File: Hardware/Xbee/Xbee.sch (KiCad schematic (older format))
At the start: 39 parts, among them J1 Alimentación, J2 Raspberry, J3 Pines 1, J4 Pines 2, J5 Programación, J6 Entrada, J7 Salida, J8 Batería, K1 SANYOU_SRD_Form_C, Q1 2N7002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

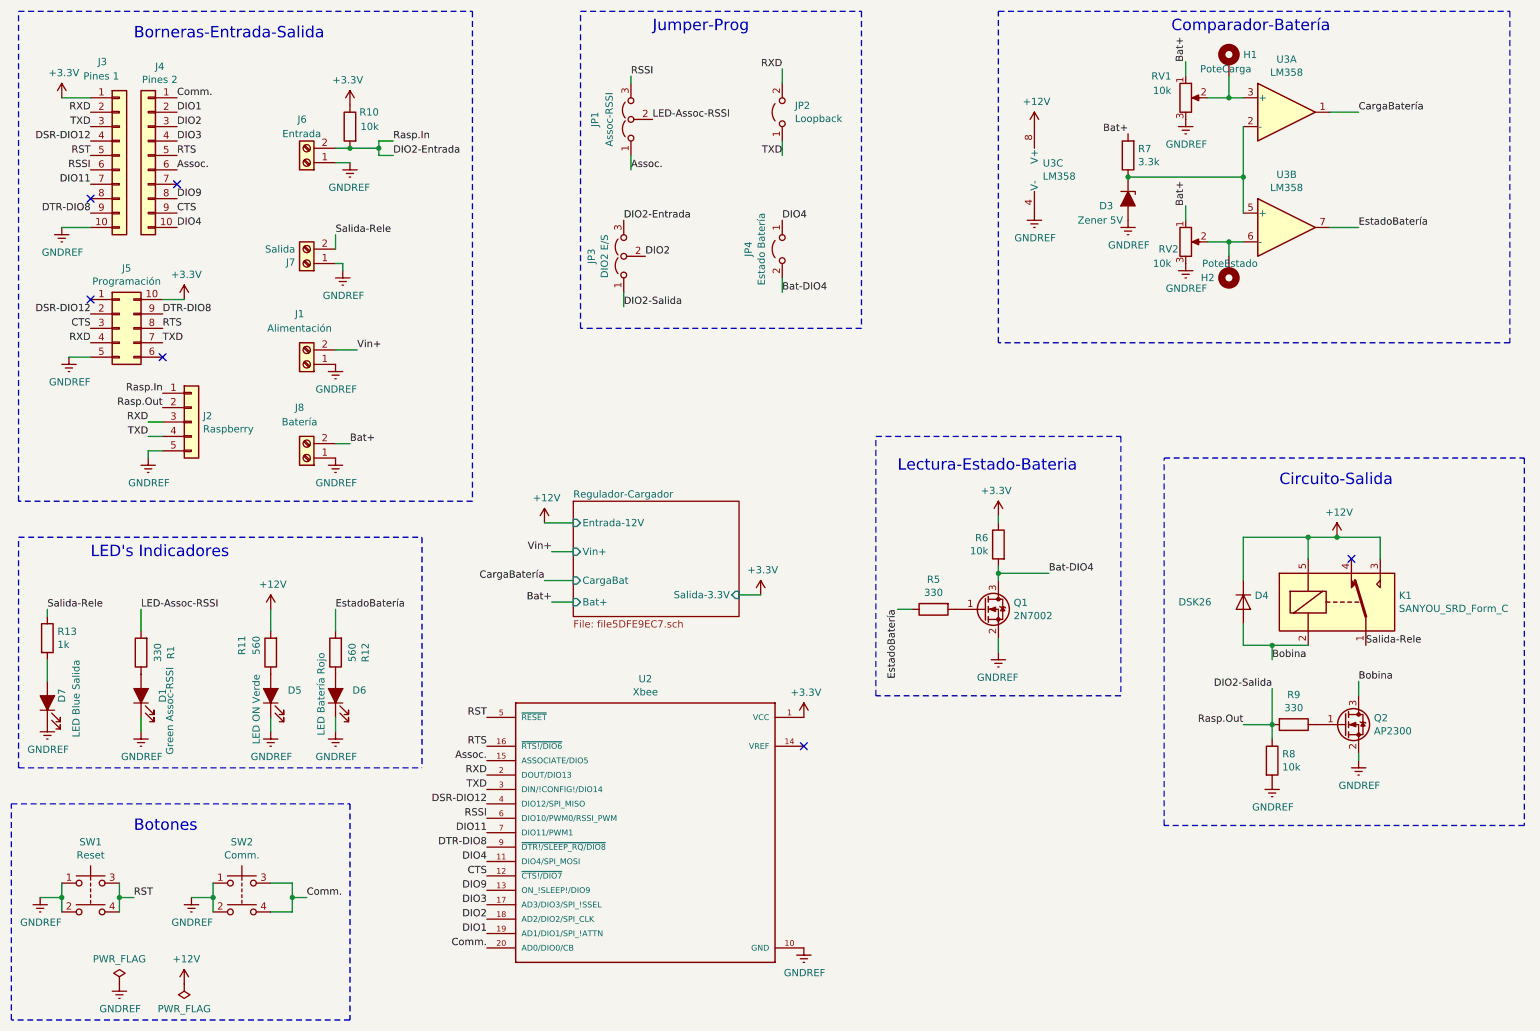
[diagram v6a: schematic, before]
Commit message: Change footprints 2
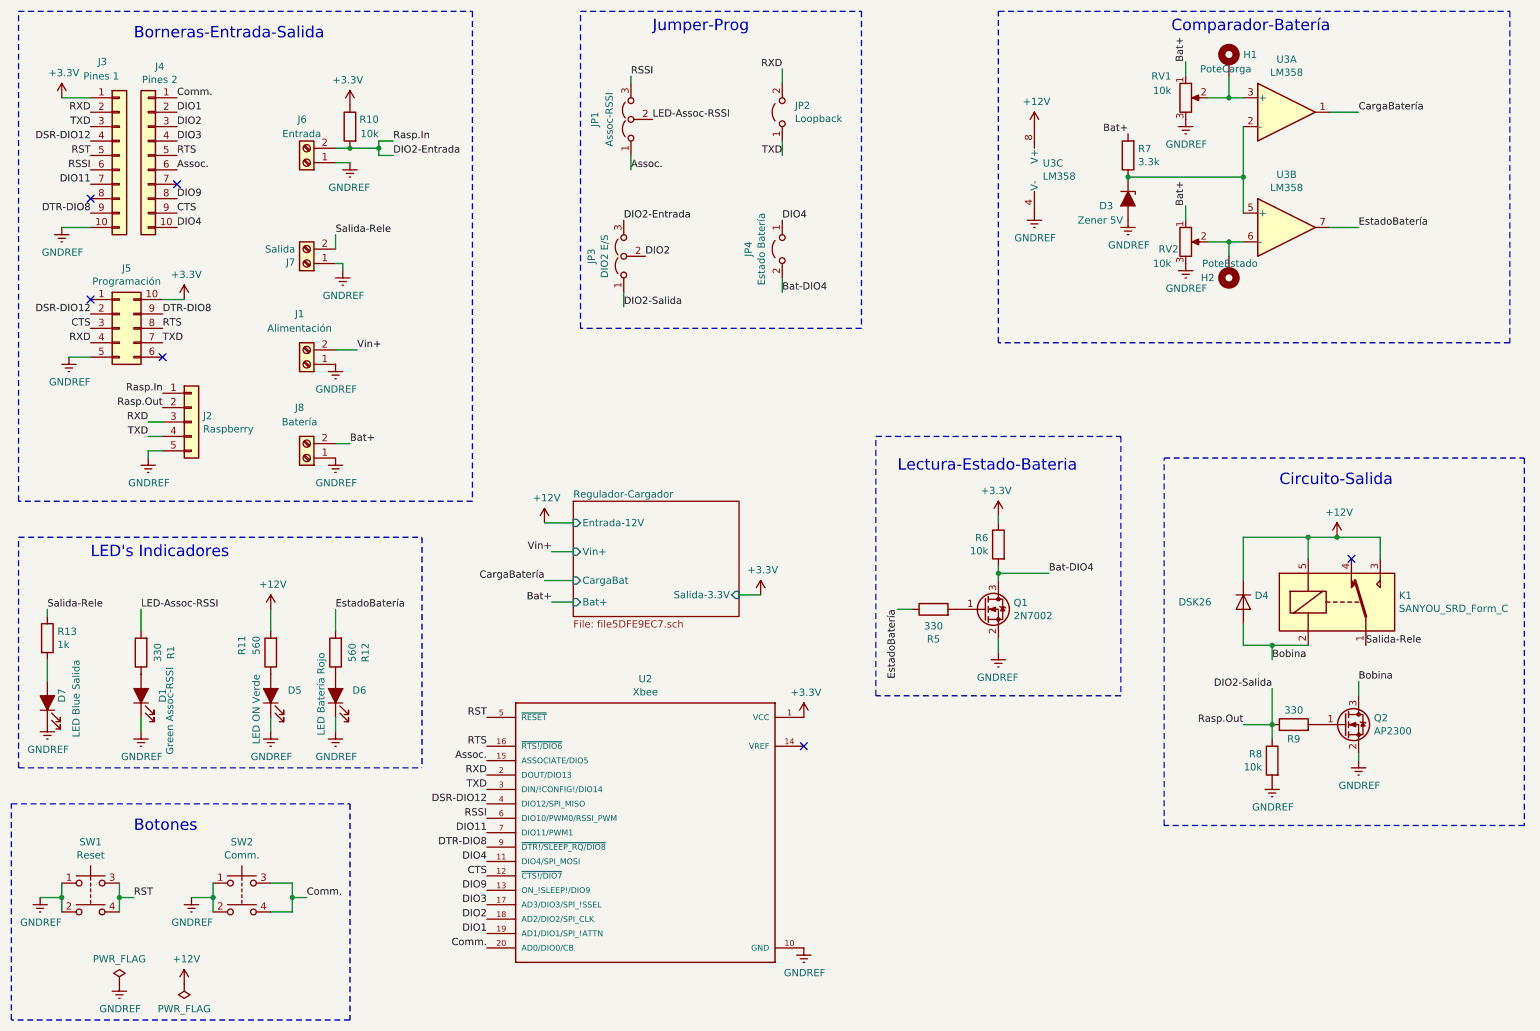
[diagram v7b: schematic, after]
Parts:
- D3: Código Proveedor 1 (none) -> 1727-5167-2-ND; Link Proveedor 1 (none) -> https://www.digikey.com/product-detail/es/nexperia-usa-inc/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; Nombre Fabricante (none) -> PLVA650A,215; Package (none) -> SOT-23
- Q1, Q2: Código Proveedor 1 (none) -> 2N7002NCT-ND; Link Proveedor 1 (none) -> https://www.digikey.com/product-detail/es/on-semiconductor/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; Nombre Fabricante (none) -> 2N7002; Package (none) -> SOT-23
- R10, R8: footprint Resistor_SMD:R_0805_2012Metric_Pad1.15x1.40mm_HandSolder -> Resistor_SMD:R_1206_3216Metric_Pad1.42x1.75mm_HandSolder; Código Proveedor 1 (none) -> 311-10KERCT-ND; Link Proveedor 1 (none) -> https://www.digikey.com/product-detail/en/yageo/RC1206JR-07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; Nombre Fabricante (none) -> RC1206JR-0710KL; Package (none) -> 1206
- R5, R9: footprint Resistor_SMD:R_0805_2012Metric_Pad1.15x1.40mm_HandSolder -> Resistor_SMD:R_1206_3216Metric_Pad1.42x1.75mm_HandSolder; Código Proveedor 1 (none) -> P.33PCT-ND; Link Proveedor 1 (none) -> https://www.digikey.com/product-detail/en/panasonic-electro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; Nombre Fabricante (none) -> ERJ-8RQJR33V; Package (none) -> 1206
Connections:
- net DIO2-Salida: now also R9.1; no longer R9.2
- net at Q2.1 (G): now also R9.2; no longer R9.1
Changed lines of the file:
@@
 EESchema Schematic File Version 4
 LIBS:Xbee-cache
-EELAYER 30 0
+EELAYER 29 0
 EELAYER END
 $Descr A4 11693 8268
@@
 F 2 "Diode_SMD:D_SOT-23_ANK" H 8350 1950 50  0001 C CNN
 F 3 "~" H 8350 1950 50  0001 C CNN
+F 4 "https://www.digikey.com/product-detail/es/nexperia-usa-inc/PLVA650A215/1727-5167-2-ND/1163688" H 8350 1950 50  0001 C CNN "Link Proveedor 1"
+F 5 "SOT-23" H 8350 1950 50  0001 C CNN "Package"
+F 6 "1727-5167-2-ND " H 8350 1950 50  0001 C CNN "Código Proveedor 1"
+F 7 "PLVA650A,215" H 8350 1950 50  0001 C CNN "Nombre Fabricante"
 	1    8350 1950
 	0    1    1    0
@@
 Wire Wire Line
 	7450 5100 7450 5000
-$Comp
-L Xbee-rescue:R-Device R5
-U 1 1 5C1B535E
-P 7000 4800
-F 0 "R5" V 6793 4800 50  0000 C CNN
-F 1 "330" V 6884 4800 50  0000 C CNN
-F 2 "Resistor_SMD:R_0805_2012Metric_Pad1.15x1.40mm_HandSolder" V 6930 4800 50  0001 C CNN
-F 3 "~" H 7000 4800 50  0001 C CNN
-	1    7000 4800
-	0    -1   1    0
-$EndComp
 Text Label 9950 2150 0    50   ~ 0
 EstadoBatería
@@
 Text Label 1750 1250 0    50   ~ 0
 Comm.
-$Comp
-L Xbee-rescue:R-Device R10
-U 1 1 5C1C2E7B
-P 2950 1450
-F 0 "R10" H 2750 1550 50  0000 L CNN
-F 1 "10k" H 2750 1450 50  0000 L CNN
-F 2 "Resistor_SMD:R_0805_2012Metric_Pad1.15x1.40mm_HandSolder" V 2880 1450 50  0001 C CNN
-F 3 "~" H 2950 1450 50  0001 C CNN
-	1    2950 1450
-	-1   0    0    -1
-$EndComp
 $Comp
 L Xbee-rescue:+3.3V-power #PWR032
@@
 	1    4850 2350
 	0    -1   -1   0
-$EndComp
-$Comp
-L Xbee-rescue:R-Device R9
-U 1 1 5C1D0264
-P 9500 5600
-F 0 "R9" V 9293 5600 50  0000 C CNN
-F 1 "330" V 9384 5600 50  0000 C CNN
-F 2 "Resistor_SMD:R_0805_2012Metric_Pad1.15x1.40mm_HandSolder" V 9430 5600 50  0001 C CNN
-F 3 "~" H 9500 5600 50  0001 C CNN
-	1    9500 5600
-	0    1    1    0
 $EndComp
 Wire Wire Line
@@
 	9150 5050 9350 5050
 $Comp
-L Xbee-rescue:R-Device R8
-U 1 1 5C89E422
-P 9350 5850
-F 0 "R8" H 9420 5896 50  0000 L CNN
-F 1 "10k" H 9420 5805 50  0000 L CNN
-F 2 "Resistor_SMD:R_0805_2012Metric_Pad1.15x1.40mm_HandSolder" V 9280 5850 50  0001 C CNN
-F 3 "~" H 9350 5850 50  0001 C CNN
-	1    9350 5850
-	1    0    0    -1
-$EndComp
-$Comp
 L Xbee-rescue:GNDREF-power #PWR027
 U 1 1 5C89E4B4
@@
 F 2 "Package_TO_SOT_SMD:SOT-23" H 7550 4725 50  0001 L CIN
 F 3 "https://www.fairchildsemi.com/datasheets/2N/2N7002.pdf" H 7350 4800 50  0001 L CNN
+F 4 "2N7002" H 7350 4800 50  0001 C CNN "Nombre Fabricante"
+F 5 "2N7002NCT-ND" H 7350 4800 50  0001 C CNN "Código Proveedor 1"
+F 6 "SOT-23" H 7350 4800 50  0001 C CNN "Package"
+F 7 "https://www.digikey.com/product-detail/es/on-semiconductor/2N7002/2N7002NCT-ND/244664" H 7350 4800 50  0001 C CNN "Link Proveedor 1"
 	1    7350 4800
 	1    0    0    -1
@@
 F 2 "Package_TO_SOT_SMD:SOT-23" H 10050 5525 50  0001 L CIN
 F 3 "https://www.fairchildsemi.com/datasheets/2N/2N7002.pdf" H 9850 5600 50  0001 L CNN
+F 4 "https://www.digikey.com/product-detail/es/on-semiconductor/2N7002/2N7002NCT-ND/244664" H 9850 5600 50  0001 C CNN "Link Proveedor 1"
+F 5 "SOT-23" H 9850 5600 50  0001 C CNN "Package"
+F 6 "2N7002" H 9850 5600 50  0001 C CNN "Nombre Fabricante"
+F 7 "2N7002NCT-ND" H 9850 5600 50  0001 C CNN "Código Proveedor 1"
 	1    9850 5600
 	1    0    0    -1
@@
 Wire Wire Line
 	3150 1650 3150 1600
-Connection ~ 2950 1600
-Wire Wire Line
-	2950 1600 2850 1600
-Wire Wire Line
-	3150 1600 2950 1600
 Connection ~ 3150 1600
 Wire Wire Line
@@
 Wire Wire Line
 	2850 4800 2850 4950
+$Comp
+L Xbee-rescue:R-Device R5
+U 1 1 5DB489D4
+P 7000 4800
+F 0 "R5" V 6793 4800 50  0000 C CNN
+F 1 "330" V 6884 4800 50  0000 C CNN
+F 2 "Resistor_SMD:R_1206_3216Metric_Pad1.42x1.75mm_HandSolder" V 6930 4800 50  0001 C CNN
+F 3 "~" H 7000 4800 50  0001 C CNN
+F 4 "ERJ-8RQJR33V" H 7000 4800 50  0001 C CNN "Nombre Fabricante"
+F 5 "P.33PCT-ND" H 7000 4800 50  0001 C CNN "Código Proveedor 1"
+F 6 "https://www.digikey.com/product-detail/en/panasonic-electronic-components/ERJ-8RQJR33V/P.33PCT-ND/250371" H 7000 4800 50  0001 C CNN "Link Proveedor 1"
+F 7 "1206" H 7000 4800 50  0001 C CNN "Package"
+	1    7000 4800
+	0    -1   -1   0
+$EndComp
+$Comp
+L Xbee-rescue:R-Device R9
+U 1 1 5DB4C324
+P 9500 5600
+F 0 "R9" V 9400 5600 50  0000 C CNN
+F 1 "330" V 9600 5600 50  0000 C CNN
+F 2 "Resistor_SMD:R_1206_3216Metric_Pad1.42x1.75mm_HandSolder" V 9430 5600 50  0001 C CNN
+F 3 "~" H 9500 5600 50  0001 C CNN
+F 4 "ERJ-8RQJR33V" H 9500 5600 50  0001 C CNN "Nombre Fabricante"
+F 5 "P.33PCT-ND" H 9500 5600 50  0001 C CNN "Código Proveedor 1"
+F 6 "https://www.digikey.com/product-detail/en/panasonic-electronic-components/ERJ-8RQJR33V/P.33PCT-ND/250371" H 9500 5600 50  0001 C CNN "Link Proveedor 1"
+F 7 "1206" H 9500 5600 50  0001 C CNN "Package"
+	1    9500 5600
+	0    -1   -1   0
+$EndComp
+$Comp
+L Xbee-rescue:R-Device R8
+U 1 1 5DB4D079
+P 9350 5850
+F 0 "R8" H 9420 5896 50  0000 L CNN
+F 1 "10k" H 9420 5805 50  0000 L CNN
+F 2 "Resistor_SMD:R_1206_3216Metric_Pad1.42x1.75mm_HandSolder" V 9280 5850 50  0001 C CNN
+F 3 "~" H 9350 5850 50  0001 C CNN
+F 4 "RC1206JR-0710KL" H 9350 5850 50  0001 C CNN "Nombre Fabricante"
+F 5 "311-10KERCT-ND" H 9350 5850 50  0001 C CNN "Código Proveedor 1"
+F 6 "https://www.digikey.com/product-detail/en/yageo/RC1206JR-0710KL/311-10KERCT-ND/732156" H 9350 5850 50  0001 C CNN "Link Proveedor 1"
+F 7 "1206" H 9350 5850 50  0001 C CNN "Package"
+	1    9350 5850
+	-1   0    0    -1
+$EndComp
+$Comp
+L Xbee-rescue:R-Device R10
+U 1 1 5DB4DBE9
+P 2950 1450
+F 0 "R10" H 2750 1500 50  0000 L CNN
+F 1 "10k" H 2750 1400 50  0000 L CNN
+F 2 "Resistor_SMD:R_1206_3216Metric_Pad1.42x1.75mm_HandSolder" V 2880 1450 50  0001 C CNN
+F 3 "~" H 2950 1450 50  0001 C CNN
+F 4 "RC1206JR-0710KL" H 2950 1450 50  0001 C CNN "Nombre Fabricante"
+F 5 "311-10KERCT-ND" H 2950 1450 50  0001 C CNN "Código Proveedor 1"
+F 6 "https://www.digikey.com/product-detail/en/yageo/RC1206JR-0710KL/311-10KERCT-ND/732156" H 2950 1450 50  0001 C CNN "Link Proveedor 1"
+F 7 "1206" H 2950 1450 50  0001 C CNN "Package"
+	1    2950 1450
+	-1   0    0    -1
+$EndComp
+Wire Wire Line
+	2850 1600 2950 1600
+Connection ~ 2950 1600
+Wire Wire Line
+	2950 1600 3150 1600
 $EndSCHEMATC

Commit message: Footprints 3
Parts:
- added H3, H4, H5, H6: MountingHole, MountingHole:MountingHole_3.2mm_M3, symbol Mechanical:MountingHole
- D3: Código Proveedor 1 1727-5167-2-ND -> BZX84C5V1LT3GOSCT-ND; Link Proveedor 1 https://www.digikey.com/product-detail/es/nexperia-usa-inc/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 -> https://www.digikey.com/product-detail/en/on-semiconductor/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; Nombre Fabricante PLVA650A,215 -> BZX84C5V1LT3G
- D4: value DSK26 -> MURA220; footprint Diode_SMD:D_SOD-123F -> Diode_SMD:D_SMA_Handsoldering; Código Proveedor 1 (none) -> MURA220T3GOSCT-ND; Link Proveedor 1 (none) -> https://www.digikey.com/product-detail/en/on-semiconductor/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; Nombre Fabricante (none) -> MURA220T3G; Package (none) -> SMA
- J1, J6, J7, J8: Código Proveedor 1 (none) -> 102-6422-ND; Código Proveedor 2 (none) -> 102-6390-ND; Link Proveedor 1 (none) -> https://www.digikey.com/product-detail/en/cui-devices/TBP01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; Link Proveedor 2 (none) -> https://www.digikey.com/product-detail/en/cui-devices/TBP01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; Nombre Fabricante (none) -> TBP01R2-508-02BE; Package (none) -> 5.08mm T/H
- J2: Código Proveedor 1 (none) -> 732-5318-ND; Link Proveedor 1 (none) -> https://www.digikey.com/product-detail/en/w-rth-elektronik/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; Nombre Fabricante (none) -> 61300511121; Package (none) -> 2.54mm T/H
- J3, J4: Código Proveedor 1 (none) -> 1212-1314-ND; Link Proveedor 1 (none) -> https://www.digikey.com/product-detail/en/831-87-010-10-001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; Nombre Fabricante (none) -> 831-87-010-10-001101; Package (none) -> 2mm T/H
- J5: footprint Connector_PinHeader_2.54mm:PinHeader_2x05_P2.54mm_Horizontal -> Connector_PinSocket_2.54mm:PinSocket_2x05_P2.54mm_Horizontal; Código Proveedor 1 (none) -> S5519-ND; Link Proveedor 1 (none) -> https://www.digikey.com/product-detail/en/sullins-connector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; Nombre Fabricante (none) -> PPTC052LJBN-RC; Package (none) -> 2.54mm T/H
- K1: value SANYOU_SRD_Form_C -> ORWH-SH-112D1F; Código Proveedor 1 (none) -> PB2029-ND; Link Proveedor 1 (none) -> https://www.digikey.com/product-detail/en/te-connectivity-p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; Nombre Fabricante (none) -> ORWH-SH-112D1F,000; Package (none) -> SPDT (1 Form C)
- SW1, SW2: Código Proveedor 1 (none) -> SW401-ND; Link Proveedor 1 (none) -> https://www.digikey.com/product-detail/en/omron-electronics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; Nombre Fabricante (none) -> B3F-1002; Package (none) -> SPST-NO
- U2: Código Proveedor 1 (none) -> 1212-1314-ND; Código Proveedor 2 (none) -> 1212-1314-ND; Link Proveedor 1 (none) -> https://www.digikey.com/product-detail/en/831-87-010-10-001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; Link Proveedor 2 (none) -> https://www.digikey.com/product-detail/en/831-87-010-10-001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; Nombre Fabricante (none) -> 831-87-010-10-001101; Package (none) -> 2mm T/H
